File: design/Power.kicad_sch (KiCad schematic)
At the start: 43 parts, among them J10 GND, J6 PH_A, J7 PH_B, J8 PH_C, J9 SUPPLY, Q1 IRF7749, Q2 IRF7749, Q3 IRF7749, Q4 IRF7749, Q5 IRF7749, Q6 IRF7749, U5 AD8418, U6 AD8418, U7 AD8418

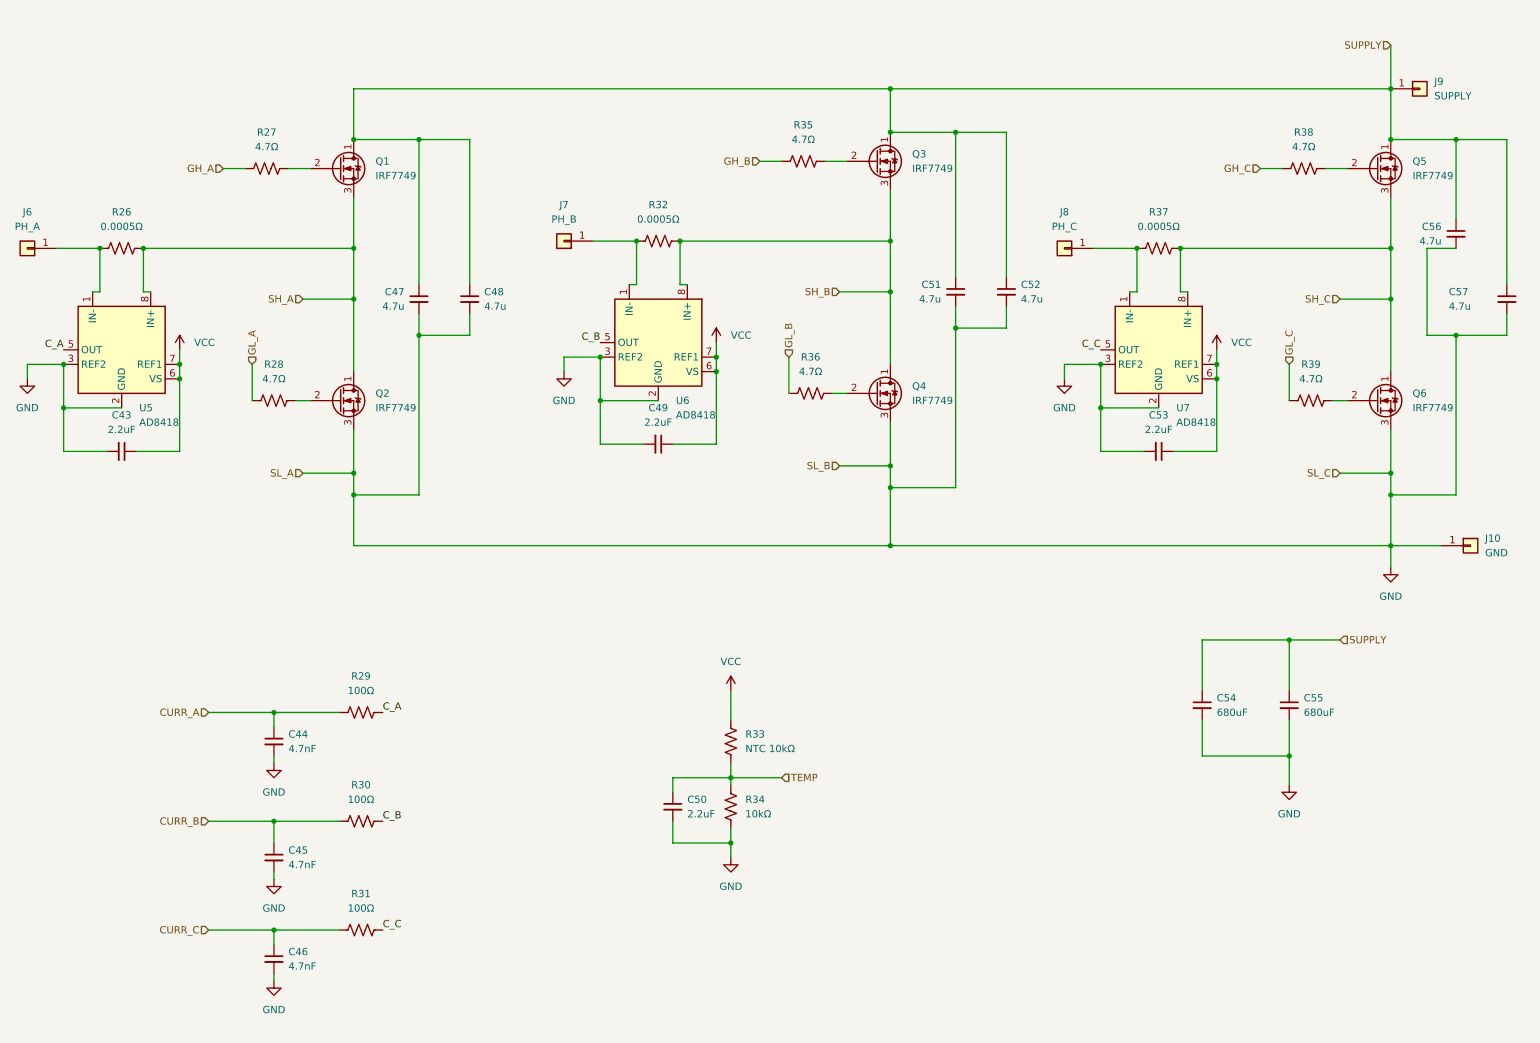
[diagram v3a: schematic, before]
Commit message: Agregado ibom
Pequeños cambios en el esquemático y agregado de ibom
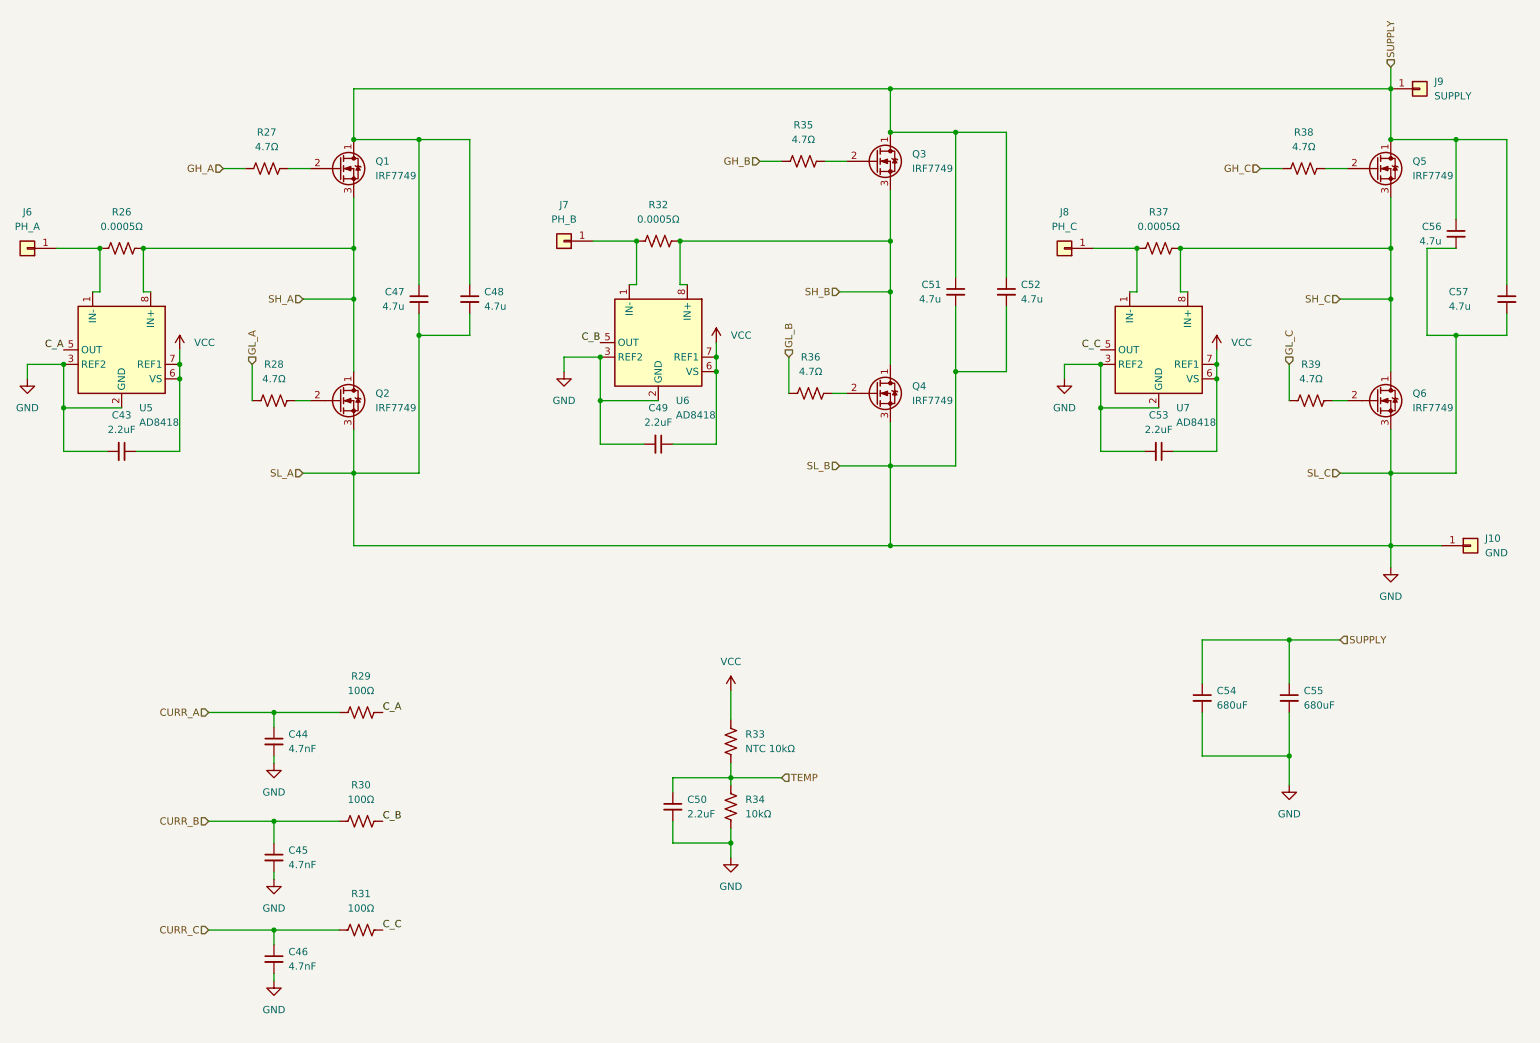
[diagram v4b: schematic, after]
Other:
- moved on the sheet: C54, C55
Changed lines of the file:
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@@
 	)
 	(junction
-		(at 170.18 97.79)
-		(diameter 0)
-		(color 0 0 0 0)
-	)
-	(junction
 		(at 133.35 54.61)
 		(diameter 0)
@@
 	)
 	(junction
+		(at 181.61 77.47)
+		(diameter 0)
+		(color 0 0 0 0)
+	)
+	(junction
 		(at 45.72 78.74)
 		(diameter 0)
@@
 	)
 	(junction
-		(at 257.81 99.06)
-		(diameter 0)
-		(color 0 0 0 0)
-	)
-	(junction
-		(at 76.2 99.06)
-		(diameter 0)
-		(color 0 0 0 0)
-	)
-	(junction
 		(at 269.24 71.12)
 		(diameter 0)
@@
 	)
 	(junction
-		(at 181.61 69.85)
-		(diameter 0)
-		(color 0 0 0 0)
-	)
-	(junction
 		(at 170.18 27.94)
 		(diameter 0)
@@
 	(wire
 		(pts
+			(xy 181.61 66.04) (xy 181.61 77.47)
+		)
+		(stroke
+			(width 0)
+			(type default)
+		)
+	)
+	(wire
+		(pts
 			(xy 170.18 54.61) (xy 170.18 63.5)
 		)
@@
 	(wire
 		(pts
-			(xy 240.03 124.46) (xy 240.03 133.35)
+			(xy 240.03 124.46) (xy 240.03 132.08)
 		)
 		(stroke
@@
 	(wire
 		(pts
-			(xy 181.61 97.79) (xy 181.61 69.85)
+			(xy 181.61 93.98) (xy 181.61 77.47)
 		)
 		(stroke
@@
 	(wire
 		(pts
-			(xy 170.18 97.79) (xy 181.61 97.79)
+			(xy 170.18 93.98) (xy 181.61 93.98)
 		)
 		(stroke
@@
 	(wire
 		(pts
-			(xy 190.5 69.85) (xy 181.61 69.85)
+			(xy 190.5 77.47) (xy 181.61 77.47)
 		)
 		(stroke
@@
 	(wire
 		(pts
-			(xy 25.4 91.44) (xy 33.02 91.44)
+			(xy 257.81 95.25) (xy 257.81 107.95)
 		)
 		(stroke
@@
 	(wire
 		(pts
-			(xy 240.03 124.46) (xy 248.92 124.46)
+			(xy 25.4 91.44) (xy 33.02 91.44)
 		)
 		(stroke
@@
 	(wire
 		(pts
-			(xy 73.66 156.21) (xy 62.23 156.21)
+			(xy 240.03 124.46) (xy 248.92 124.46)
 		)
 		(stroke
@@
 	(wire
 		(pts
-			(xy 139.7 77.47) (xy 139.7 90.17)
+			(xy 73.66 156.21) (xy 62.23 156.21)
 		)
 		(stroke
@@
 	(wire
 		(pts
-			(xy 119.38 82.55) (xy 119.38 90.17)
+			(xy 139.7 77.47) (xy 139.7 90.17)
 		)
 		(stroke
@@
 	(wire
 		(pts
-			(xy 62.23 175.26) (xy 50.8 175.26)
+			(xy 119.38 82.55) (xy 119.38 90.17)
 		)
 		(stroke
@@
 	(wire
 		(pts
-			(xy 161.29 93.98) (xy 170.18 93.98)
+			(xy 62.23 175.26) (xy 50.8 175.26)
 		)
 		(stroke
@@
 	(wire
 		(pts
-			(xy 76.2 95.25) (xy 76.2 99.06)
+			(xy 161.29 93.98) (xy 170.18 93.98)
 		)
 		(stroke
@@
 	(wire
 		(pts
-			(xy 224.79 138.43) (xy 224.79 144.78)
+			(xy 224.79 137.16) (xy 224.79 144.78)
 		)
 		(stroke
@@
 	(wire
 		(pts
-			(xy 170.18 93.98) (xy 170.18 97.79)
-		)
-		(stroke
-			(width 0)
-			(type default)
-		)
-	)
-	(wire
-		(pts
 			(xy 45.72 73.66) (xy 45.72 76.2)
 		)
@@
 	(wire
 		(pts
-			(xy 257.81 20.32) (xy 257.81 27.94)
+			(xy 257.81 24.13) (xy 257.81 27.94)
 		)
 		(stroke
@@
 	(wire
 		(pts
-			(xy 269.24 99.06) (xy 269.24 71.12)
+			(xy 269.24 95.25) (xy 269.24 71.12)
 		)
 		(stroke
@@
 	(wire
 		(pts
-			(xy 87.63 99.06) (xy 87.63 71.12)
+			(xy 87.63 95.25) (xy 87.63 71.12)
 		)
 		(stroke
@@
 	(wire
 		(pts
-			(xy 170.18 97.79) (xy 170.18 107.95)
+			(xy 170.18 93.98) (xy 170.18 107.95)
 		)
 		(stroke
@@
 	(wire
 		(pts
-			(xy 257.81 95.25) (xy 257.81 99.06)
-		)
-		(stroke
-			(width 0)
-			(type default)
-		)
-	)
-	(wire
-		(pts
 			(xy 57.15 41.91) (xy 53.34 41.91)
 		)
@@
 	(wire
 		(pts
-			(xy 257.81 99.06) (xy 257.81 107.95)
-		)
-		(stroke
-			(width 0)
-			(type default)
-		)
-	)
-	(wire
-		(pts
 			(xy 227.33 73.66) (xy 227.33 76.2)
 		)
@@
 	(wire
 		(pts
-			(xy 181.61 66.04) (xy 181.61 69.85)
-		)
-		(stroke
-			(width 0)
-			(type default)
-		)
-	)
-	(wire
-		(pts
 			(xy 142.24 160.02) (xy 142.24 162.56)
 		)
@@
 	(wire
 		(pts
-			(xy 76.2 99.06) (xy 87.63 99.06)
+			(xy 76.2 95.25) (xy 87.63 95.25)
 		)
 		(stroke
@@
 	(wire
 		(pts
-			(xy 190.5 66.04) (xy 190.5 69.85)
+			(xy 190.5 66.04) (xy 190.5 77.47)
 		)
 		(stroke
@@
 	(wire
 		(pts
-			(xy 224.79 124.46) (xy 224.79 133.35)
+			(xy 224.79 124.46) (xy 224.79 132.08)
 		)
 		(stroke
@@
 	(wire
 		(pts
-			(xy 76.2 99.06) (xy 76.2 107.95)
-		)
-		(stroke
-			(width 0)
-			(type default)
-		)
-	)
-	(wire
-		(pts
 			(xy 257.81 107.95) (xy 266.7 107.95)
 		)
@@
 	(wire
 		(pts
-			(xy 257.81 99.06) (xy 269.24 99.06)
+			(xy 257.81 95.25) (xy 269.24 95.25)
 		)
 		(stroke
@@
 	(wire
 		(pts
+			(xy 76.2 95.25) (xy 76.2 107.95)
+		)
+		(stroke
+			(width 0)
+			(type default)
+		)
+	)
+	(wire
+		(pts
 			(xy 170.18 45.72) (xy 170.18 54.61)
 		)
@@
 	(wire
 		(pts
-			(xy 240.03 138.43) (xy 240.03 144.78)
+			(xy 240.03 137.16) (xy 240.03 144.78)
 		)
 		(stroke
@@
 	(hierarchical_label "SUPPLY"
 		(shape input)
-		(at 257.81 20.32 180)
+		(at 257.81 24.13 90)
 		(fields_autoplaced yes)
 		(effects
@@
 				(size 1.27 1.27)
 			)
-			(justify right)
+			(justify left)
 		)
 	)
@@
 	(symbol
 		(lib_id "Device:C_Small")
-		(at 224.79 135.89 0)
+		(at 224.79 134.62 0)
 		(unit 1)
 		(exclude_from_sim no)
@@
 		(fields_autoplaced yes)
 		(property "Reference" "C54"
-			(at 227.33 134.6262 0)
+			(at 227.33 133.3562 0)
 			(effects
 				(font
@@
 		)
 		(property "Value" "680uF"
-			(at 227.33 137.1662 0)
+			(at 227.33 135.8962 0)
 			(effects
 				(font
@@
 		)
 		(property "Footprint" "Capacitor_THT:CP_Radial_D6.3mm_P2.50mm"
-			(at 224.79 135.89 0)
+			(at 224.79 134.62 0)
 			(effects
 				(font
@@
 		)
 		(property "Datasheet" "~"
-			(at 224.79 135.89 0)
+			(at 224.79 134.62 0)
 			(effects
 				(font
@@
 		)
 		(property "Description" "CAP ALUM 680UF 20% 80V"
-			(at 224.79 135.89 0)
+			(at 224.79 134.62 0)
 			(effects
 				(font
@@
 	(symbol
 		(lib_id "Device:C_Small")
-		(at 240.03 135.89 0)
+		(at 240.03 134.62 0)
 		(unit 1)
 		(exclude_from_sim no)
@@
 		(fields_autoplaced yes)
 		(property "Reference" "C55"
-			(at 242.57 134.6262 0)
+			(at 242.57 133.3562 0)
 			(effects
 				(font
@@
 		)
 		(property "Value" "680uF"
-			(at 242.57 137.1662 0)
+			(at 242.57 135.8962 0)
 			(effects
 				(font
@@
 		)
 		(property "Footprint" "Capacitor_THT:CP_Radial_D6.3mm_P2.50mm"
-			(at 240.03 135.89 0)
+			(at 240.03 134.62 0)
 			(effects
 				(font
@@
 		)
 		(property "Datasheet" "~"
-			(at 240.03 135.89 0)
+			(at 240.03 134.62 0)
 			(effects
 				(font
@@
 		)
 		(property "Description" "CAP ALUM 680UF 20% 80V"
-			(at 240.03 135.89 0)
+			(at 240.03 134.62 0)
 			(effects
 				(font

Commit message: Cambios en el esquemático
- Cambio de Vcc por +3.3V
- Agregado de hoja para desarrollar la entrada de tensión alterna
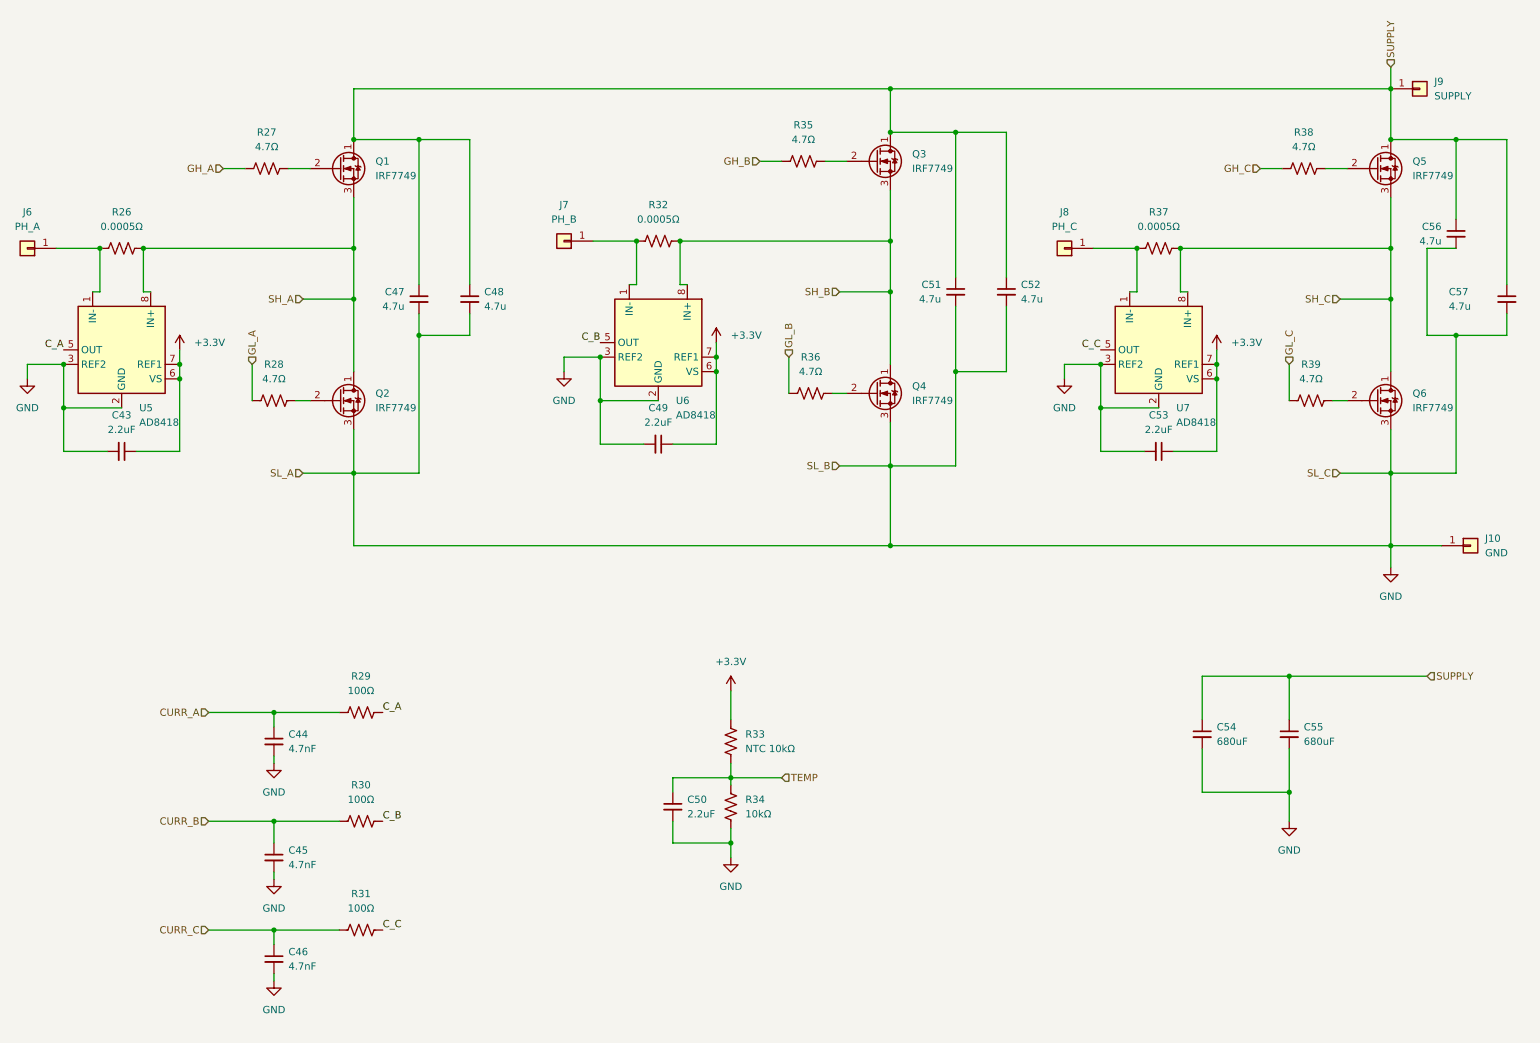
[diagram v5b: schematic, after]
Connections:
- net VCC renamed +3.3V
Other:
- moved on the sheet: C54, C55
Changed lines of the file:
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@@
 	)
 	(junction
+		(at 240.03 130.81)
+		(diameter 0)
+		(color 0 0 0 0)
+	)
+	(junction
 		(at 257.81 27.94)
 		(diameter 0)
@@
 	)
 	(junction
-		(at 240.03 124.46)
-		(diameter 0)
-		(color 0 0 0 0)
-	)
-	(junction
 		(at 170.18 27.94)
 		(diameter 0)
@@
 	)
 	(junction
-		(at 240.03 144.78)
+		(at 240.03 151.13)
 		(diameter 0)
 		(color 0 0 0 0)
@@
 	(wire
 		(pts
+			(xy 240.03 130.81) (xy 264.16 130.81)
+		)
+		(stroke
+			(width 0)
+			(type default)
+		)
+	)
+	(wire
+		(pts
 			(xy 142.24 133.35) (xy 142.24 138.43)
 		)
@@
 	(wire
 		(pts
-			(xy 240.03 124.46) (xy 240.03 132.08)
+			(xy 240.03 130.81) (xy 240.03 138.43)
 		)
 		(stroke
@@
 	(wire
 		(pts
-			(xy 224.79 144.78) (xy 240.03 144.78)
+			(xy 224.79 151.13) (xy 240.03 151.13)
 		)
 		(stroke
@@
 	(wire
 		(pts
-			(xy 240.03 124.46) (xy 248.92 124.46)
+			(xy 240.03 130.81) (xy 224.79 130.81)
 		)
 		(stroke
@@
 	(wire
 		(pts
-			(xy 224.79 137.16) (xy 224.79 144.78)
+			(xy 224.79 143.51) (xy 224.79 151.13)
 		)
 		(stroke
@@
 	(wire
 		(pts
-			(xy 240.03 144.78) (xy 240.03 149.86)
+			(xy 240.03 151.13) (xy 240.03 156.21)
 		)
 		(stroke
@@
 	(wire
 		(pts
-			(xy 224.79 124.46) (xy 224.79 132.08)
+			(xy 224.79 130.81) (xy 224.79 138.43)
 		)
 		(stroke
@@
 	(wire
 		(pts
-			(xy 224.79 124.46) (xy 240.03 124.46)
-		)
-		(stroke
-			(width 0)
-			(type default)
-		)
-	)
-	(wire
-		(pts
 			(xy 125.73 54.61) (xy 125.73 62.23)
 		)
@@
 	(wire
 		(pts
-			(xy 240.03 137.16) (xy 240.03 144.78)
+			(xy 240.03 143.51) (xy 240.03 151.13)
 		)
 		(stroke
@@
 	(hierarchical_label "SUPPLY"
 		(shape input)
-		(at 248.92 124.46 0)
+		(at 264.16 130.81 0)
 		(fields_autoplaced yes)
 		(effects
@@
 			)
 		)
-		(property "Value" "VCC"
+		(property "Value" "+3.3V"
 			(at 142.24 71.1199 0)
 			(effects
@@
 			)
 		)
-		(property "Value" "VCC"
+		(property "Value" "+3.3V"
 			(at 48.26 72.3899 0)
 			(effects
@@
 			)
 		)
-		(property "Value" "VCC"
+		(property "Value" "+3.3V"
 			(at 229.87 72.3899 0)
 			(effects
@@
 			)
 		)
-		(property "Value" "VCC"
+		(property "Value" "+3.3V"
 			(at 142.24 128.27 0)
 			(effects
@@
 	(symbol
 		(lib_id "Device:C_Small")
-		(at 224.79 134.62 0)
+		(at 224.79 140.97 0)
 		(unit 1)
 		(exclude_from_sim no)
@@
 		(fields_autoplaced yes)
 		(property "Reference" "C54"
-			(at 227.33 133.3562 0)
+			(at 227.33 139.7062 0)
 			(effects
 				(font
@@
 		)
 		(property "Value" "680uF"
-			(at 227.33 135.8962 0)
+			(at 227.33 142.2462 0)
 			(effects
 				(font
@@
 		)
 		(property "Footprint" "Capacitor_THT:CP_Radial_D6.3mm_P2.50mm"
-			(at 224.79 134.62 0)
+			(at 224.79 140.97 0)
 			(effects
 				(font
@@
 		)
 		(property "Datasheet" "~"
-			(at 224.79 134.62 0)
+			(at 224.79 140.97 0)
 			(effects
 				(font
@@
 		)
 		(property "Description" "CAP ALUM 680UF 20% 80V"
-			(at 224.79 134.62 0)
+			(at 224.79 140.97 0)
 			(effects
 				(font
@@
 	(symbol
 		(lib_id "Device:C_Small")
-		(at 240.03 134.62 0)
+		(at 240.03 140.97 0)
 		(unit 1)
 		(exclude_from_sim no)
@@
 		(fields_autoplaced yes)
 		(property "Reference" "C55"
-			(at 242.57 133.3562 0)
+			(at 242.57 139.7062 0)
 			(effects
 				(font
@@
 		)
 		(property "Value" "680uF"
-			(at 242.57 135.8962 0)
+			(at 242.57 142.2462 0)
 			(effects
 				(font
@@
 		)
 		(property "Footprint" "Capacitor_THT:CP_Radial_D6.3mm_P2.50mm"
-			(at 240.03 134.62 0)
+			(at 240.03 140.97 0)
 			(effects
 				(font
@@
 		)
 		(property "Datasheet" "~"
-			(at 240.03 134.62 0)
+			(at 240.03 140.97 0)
 			(effects
 				(font
@@
 		)
 		(property "Description" "CAP ALUM 680UF 20% 80V"
-			(at 240.03 134.62 0)
+			(at 240.03 140.97 0)
 			(effects
 				(font
@@
 	(symbol
 		(lib_id "power:GND")
-		(at 240.03 149.86 0)
+		(at 240.03 156.21 0)
 		(unit 1)
 		(exclude_from_sim no)
@@
 		(fields_autoplaced yes)
 		(property "Reference" "#PWR080"
-			(at 240.03 156.21 0)
+			(at 240.03 162.56 0)
 			(effects
 				(font
@@
 		)
 		(property "Value" "GND"
-			(at 240.03 154.94 0)
+			(at 240.03 161.29 0)
 			(effects
 				(font
@@
 		)
 		(property "Footprint" ""
-			(at 240.03 149.86 0)
+			(at 240.03 156.21 0)
 			(effects
 				(font
@@
 		)
 		(property "Datasheet" ""
-			(at 240.03 149.86 0)
+			(at 240.03 156.21 0)
 			(effects
 				(font
@@
 		)
 		(property "Description" "Power symbol creates a global label with name \"GND\" , ground"
-			(at 240.03 149.86 0)
+			(at 240.03 156.21 0)
 			(effects
 				(font

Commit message: Commit antes del merge
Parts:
- removed C50: 2.2uF, Capacitor_SMD:C_0603_1608Metric, symbol Device:C_Small
- removed C54, C55: 680uF, Capacitor_THT:CP_Radial_D6.3mm_P2.50mm, symbol Device:C_Small
- added C1: 4.7nF, Capacitor_SMD:C_0603_1608Metric, symbol Device:C_Small
- added R17, R19, R4: 39kΩ, Resistor_SMD:R_0603_1608Metric, symbol Device:R_US
- added R20, R21, R23, R40: 2k2Ω, Resistor_SMD:R_0603_1608Metric, symbol Device:R_US
- added R24: 100Ω, Resistor_SMD:R_0603_1608Metric, symbol Device:R_US
- C46: value 4.7nF -> 2.2uF
- R31: value 100Ω -> NTC 10kΩ
- R33: value NTC 10kΩ -> 10kΩ
- R34: value 10kΩ -> 39kΩ
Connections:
- net +3.3V: now also R31.1; no longer R33.1
- net CURR_A: now also C1.1, R24.2; no longer C44.1, R29.2
- net CURR_B: now also C44.1, R29.2; no longer C45.1, R30.2
- net CURR_C: now also C45.1, R30.2; no longer C46.1, R31.2
- net C_A: now also R24.1; no longer R29.1
- net C_B: now also R29.1; no longer R30.1
- net C_C: now also R30.1; no longer R31.1
- net GND: now also R33.2, C1.2, R20.1, R21.1, R23.1, R40.1; no longer R34.2
- net SH_A: now also R4.1
- net SH_B: now also R34.1
- net SH_C: now also R17.1
- net SUPPLY: now also R19.1
- net TEMP: now also C46.1, R31.2, R33.1; no longer R33.2, R34.1
- new net SENS_A: R20.2, R4.2
- new net SENS_B: R34.2, R40.2
- new net SENS_C: R17.2, R21.2
- new net SENS_SUPPLY: R19.2, R23.2
